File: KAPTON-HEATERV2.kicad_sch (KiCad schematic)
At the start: 18 parts, among them J1 XT60PW-M, J2 XT60PW-M, J3 1985276, J4 1985218, J5 10090926-P154XLF, K1 1-1393210-8, Q1 AO3400A, U1 TC4427ACOA

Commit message: finalized?
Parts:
- removed C1: C0.1uf, Capacitor_SMD:C_0805_2012Metric, symbol Device:C
- removed C2: C47uf, Capacitor_THT:CP_Radial_D6.3mm_P2.50mm, symbol Device:C
- removed C3: C1uf, Capacitor_SMD:C_0805_2012Metric, symbol Device:C
- added R4: 4.7k, symbol Device:R
- added R5: 10k, symbol Device:R
- C4: value C10uf -> C47.5nf; footprint Capacitor_THT:CP_Radial_D6.3mm_P2.50mm -> Capacitor_SMD:C_0805_2012Metric
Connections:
- net 10V PWM: now also R5.1
- net 5V: now also D1.1 (K); no longer D1.2 (A)
- net GND: now also R4.2, R5.2
- net at K1.2, Q1.2: now also D1.2 (A); no longer D1.1 (K)
- net at Q1.1, R1.2: now also R4.1
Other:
- note removed: "Decoupling capacitors"
- moved on the sheet: C4, D1

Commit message: forgot to save sch
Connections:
- net 5V: now also J5.11; no longer J5.10
- net GND: now also J5.10; no longer J5.11
- net TH6: now also J5.15; no longer J5.6
- net TH7: now also J5.14; no longer J5.7
- net TH8: now also J5.13; no longer J5.8
- net TH9: now also J5.12; no longer J5.9

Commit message: added resistors to pcb
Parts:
- R4, R5: footprint (none) -> PCM_JLCPCB:R_1206
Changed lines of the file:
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@@
 			)
 		)
-		(property "Footprint" ""
+		(property "Footprint" "PCM_JLCPCB:R_1206"
 			(at 144.272 95.25 90)
 			(effects
@@
 			)
 		)
-		(property "Footprint" ""
+		(property "Footprint" "PCM_JLCPCB:R_1206"
 			(at 82.042 35.56 90)
 			(effects

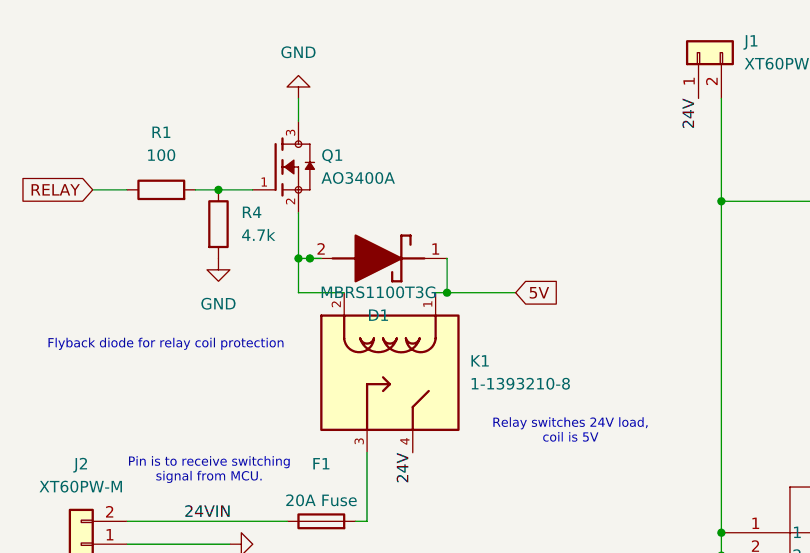
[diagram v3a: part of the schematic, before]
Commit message: fixed a trace
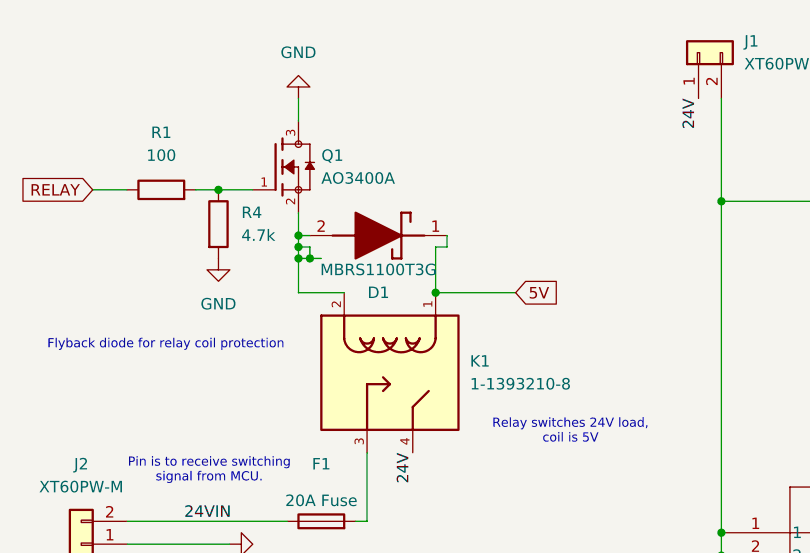
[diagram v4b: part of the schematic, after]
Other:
- moved on the sheet: D1
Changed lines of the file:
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@@
+	)
+	(junction
+		(at 107.95 43.18)
+		(diameter 0)
+		(color 0 0 0 0)
 	)
 	(junction
@@
 	)
 	(junction
-		(at 109.22 43.18)
-		(diameter 0)
-		(color 0 0 0 0)
-	)
-	(junction
 		(at 92.71 39.37)
 		(diameter 0)
@@
 	)
 	(junction
+		(at 92.71 38.1)
+		(diameter 0)
+		(color 0 0 0 0)
+	)
+	(junction
+		(at 92.71 36.83)
+		(diameter 0)
+		(color 0 0 0 0)
+	)
+	(junction
 		(at 93.98 39.37)
 		(diameter 0)
@@
 	(wire
 		(pts
+			(xy 92.71 38.1) (xy 92.71 39.37)
+		)
+		(stroke
+			(width 0)
+			(type default)
+		)
+	)
+	(wire
+		(pts
 			(xy 95.25 39.37) (xy 93.98 39.37)
 		)
@@
 	(wire
 		(pts
+			(xy 93.98 36.83) (xy 92.71 36.83)
+		)
+		(stroke
+			(width 0)
+			(type default)
+		)
+	)
+	(wire
+		(pts
 			(xy 146.05 91.44) (xy 138.43 91.44)
 		)
@@
 	(wire
 		(pts
-			(xy 107.95 43.18) (xy 109.22 43.18)
+			(xy 107.95 43.18) (xy 116.84 43.18)
 		)
 		(stroke
@@
 	(wire
 		(pts
+			(xy 92.71 38.1) (xy 93.98 38.1)
+		)
+		(stroke
+			(width 0)
+			(type default)
+		)
+	)
+	(wire
+		(pts
 			(xy 87.63 88.9) (xy 96.52 88.9)
 		)
@@
 	(wire
 		(pts
+			(xy 92.71 36.83) (xy 92.71 38.1)
+		)
+		(stroke
+			(width 0)
+			(type default)
+		)
+	)
+	(wire
+		(pts
 			(xy 100.33 68.58) (xy 99.06 68.58)
 		)
@@
 	(wire
 		(pts
+			(xy 107.95 38.1) (xy 107.95 43.18)
+		)
+		(stroke
+			(width 0)
+			(type default)
+		)
+	)
+	(wire
+		(pts
 			(xy 81.28 31.75) (xy 83.82 31.75)
 		)
@@
 	(wire
 		(pts
-			(xy 109.22 39.37) (xy 109.22 43.18)
-		)
-		(stroke
-			(width 0)
-			(type default)
-		)
-	)
-	(wire
-		(pts
-			(xy 109.22 43.18) (xy 116.84 43.18)
+			(xy 109.22 36.83) (xy 109.22 38.1)
 		)
 		(stroke
@@
 	(wire
 		(pts
+			(xy 109.22 38.1) (xy 107.95 38.1)
+		)
+		(stroke
+			(width 0)
+			(type default)
+		)
+	)
+	(wire
+		(pts
 			(xy 139.7 21.59) (xy 139.7 33.02)
 		)
@@
 	(wire
 		(pts
-			(xy 92.71 34.29) (xy 92.71 39.37)
+			(xy 92.71 34.29) (xy 92.71 36.83)
 		)
 		(stroke
@@
 		(pts
 			(xy 93.98 39.37) (xy 92.71 39.37)
+		)
+		(stroke
+			(width 0)
+			(type default)
+		)
+	)
+	(wire
+		(pts
+			(xy 93.98 38.1) (xy 93.98 39.37)
 		)
 		(stroke
@@
 	(symbol
 		(lib_id "MBRS1100T3G:MBRS1100T3G")
-		(at 111.76 39.37 180)
+		(at 111.76 36.83 180)
 		(unit 1)
 		(exclude_from_sim no)
@@
 		(dnp no)
 		(property "Reference" "D1"
-			(at 101.6 45.72 0)
+			(at 101.6 43.18 0)
 			(effects
 				(font
@@
 		)
 		(property "Value" "MBRS1100T3G"
-			(at 101.6 43.18 0)
+			(at 101.6 40.64 0)
 			(effects
 				(font
@@
 		)
 		(property "Footprint" "MBRS1100T3G:DIOM5436X247N"
-			(at 99.06 -54.28 0)
+			(at 99.06 -56.82 0)
 			(effects
 				(font
@@
 		)
 		(property "Datasheet" "https://www.onsemi.com/pub/Collateral/MBRS1100T3-D.PDF"
-			(at 99.06 -154.28 0)
+			(at 99.06 -156.82 0)
 			(effects
 				(font
@@
 		)
 		(property "Description" "Weight: 95 mg (approximately); Rectangular Package for Automated Handling; Case: Epoxy, Molded; Markings: MBRS190T3: B19 MBRS1100T3: B1C; Cathode Polarity Band; Lead and Mounting Surface Temperature for Soldering Purposes: 260C Max. for 10 Seconds; Shipped in 12 mm Tape and Reel, 2500 units per reel; 150C Operating Junction Temperature; Finish: All External Surfaces Corrosion Resistant and Terminal Leads are Readily Solderable; Small Compact Surface Mountable Package with J-Bend Leads; Highly Stable Oxide"
-			(at 111.76 39.37 0)
+			(at 111.76 36.83 0)
 			(effects
 				(font
@@
 		)
 		(property "Height" "2.47"
-			(at 99.06 -354.28 0)
+			(at 99.06 -356.82 0)
 			(effects
 				(font
@@
 		)
 		(property "Mouser Part Number" "863-MBRS1100T3G"
-			(at 99.06 -454.28 0)
+			(at 99.06 -456.82 0)
 			(effects
 				(font
@@
 		)
 		(property "Mouser Price/Stock" "https://www.mouser.co.uk/ProductDetail/onsemi/MBRS1100T3G?qs=3JMERSakebpsze4F2qcnhA%3D%3D"
-			(at 99.06 -554.28 0)
+			(at 99.06 -556.82 0)
 			(effects
 				(font
@@
 		)
 		(property "Manufacturer_Name" "onsemi"
-			(at 99.06 -654.28 0)
+			(at 99.06 -656.82 0)
 			(effects
 				(font
@@
 		)
 		(property "Manufacturer_Part_Number" "MBRS1100T3G"
-			(at 99.06 -754.28 0)
-			(effects
-				(font
+			(at 99.06 -756.82 0)
+			(effects
+				(font

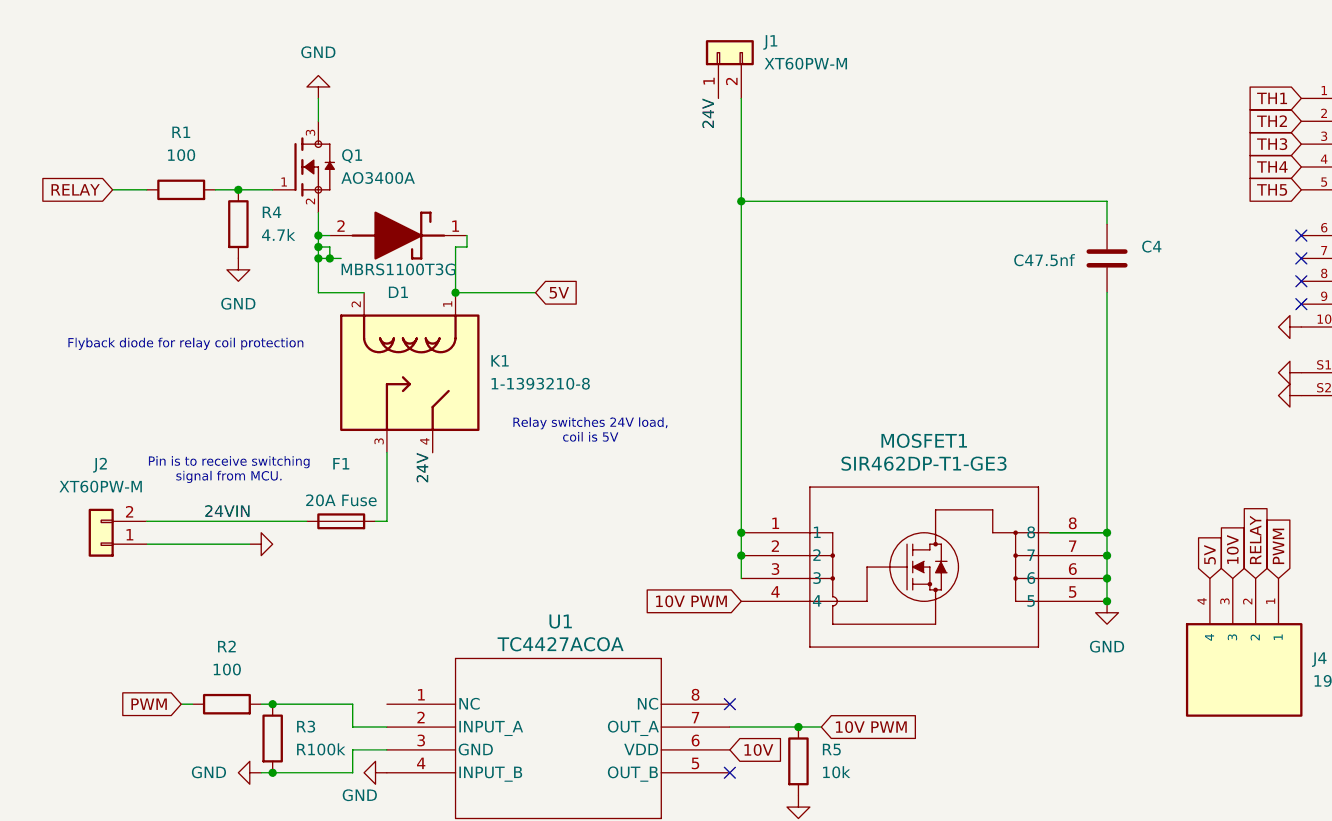
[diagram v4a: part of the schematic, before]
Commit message: fixed the mosfet
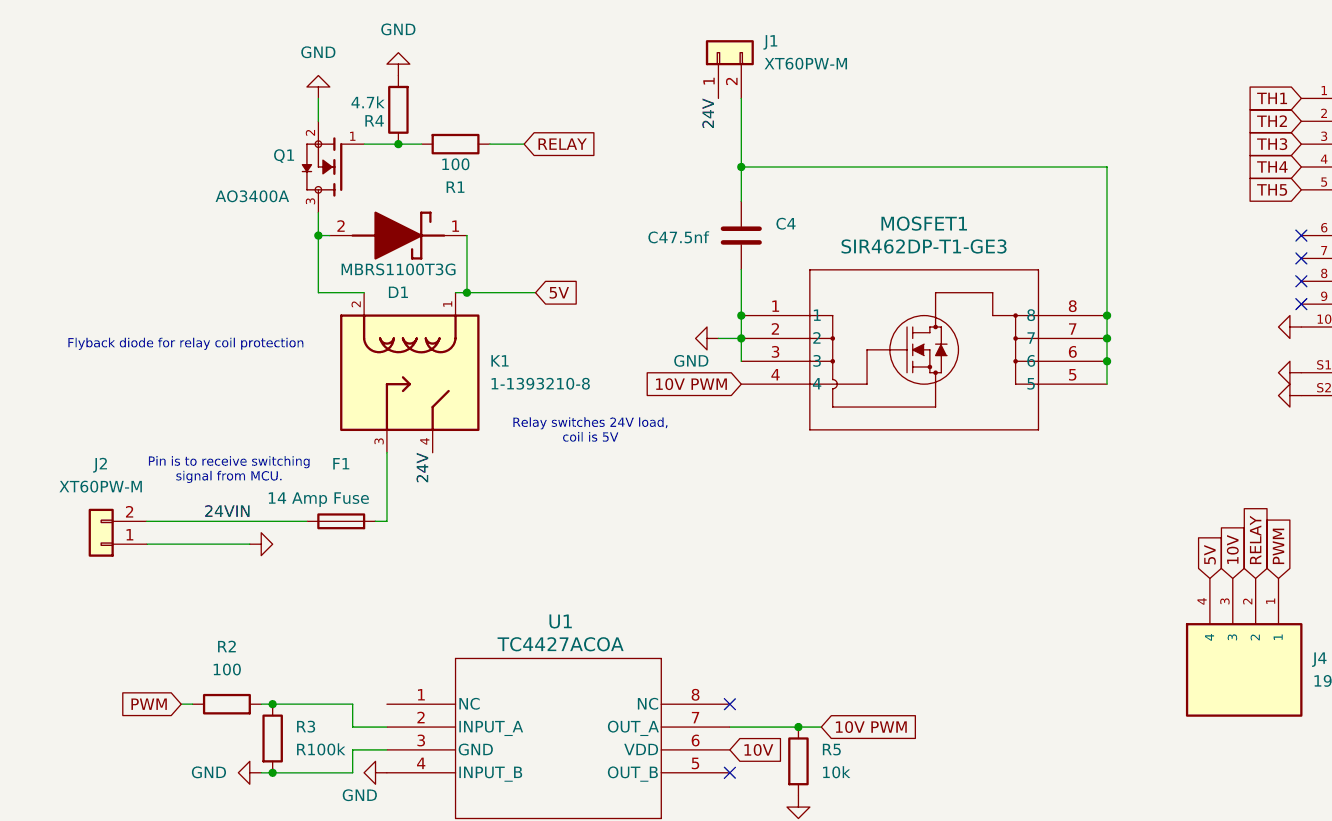
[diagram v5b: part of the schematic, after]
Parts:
- F1: value 20A Fuse -> 14 Amp Fuse
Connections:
- net GND: now also MOSFET1.1, MOSFET1.2, MOSFET1.3, Q1.2; no longer MOSFET1.5, MOSFET1.6, MOSFET1.7, MOSFET1.8, Q1.3
- net at D1.2 (A), K1.2: now also Q1.3; no longer Q1.2
- new net: C4.2, J1.2 (Pin_2), MOSFET1.5, MOSFET1.6, MOSFET1.7, MOSFET1.8
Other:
- moved on the sheet: C4, MOSFET1, Q1, R1, R4

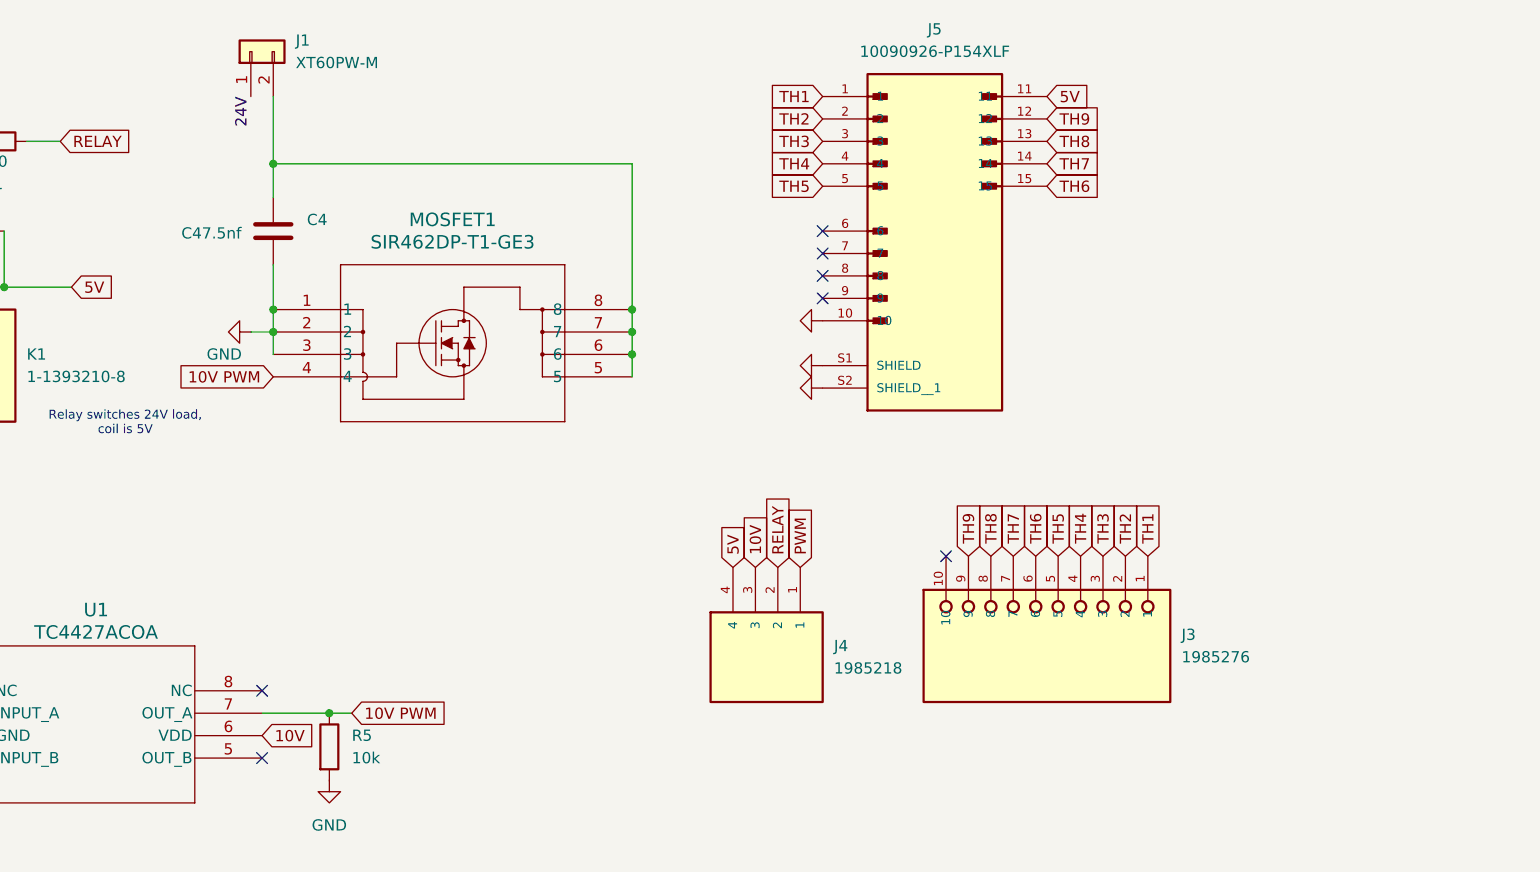
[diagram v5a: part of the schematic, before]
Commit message: added shunt resistor, fixed caps
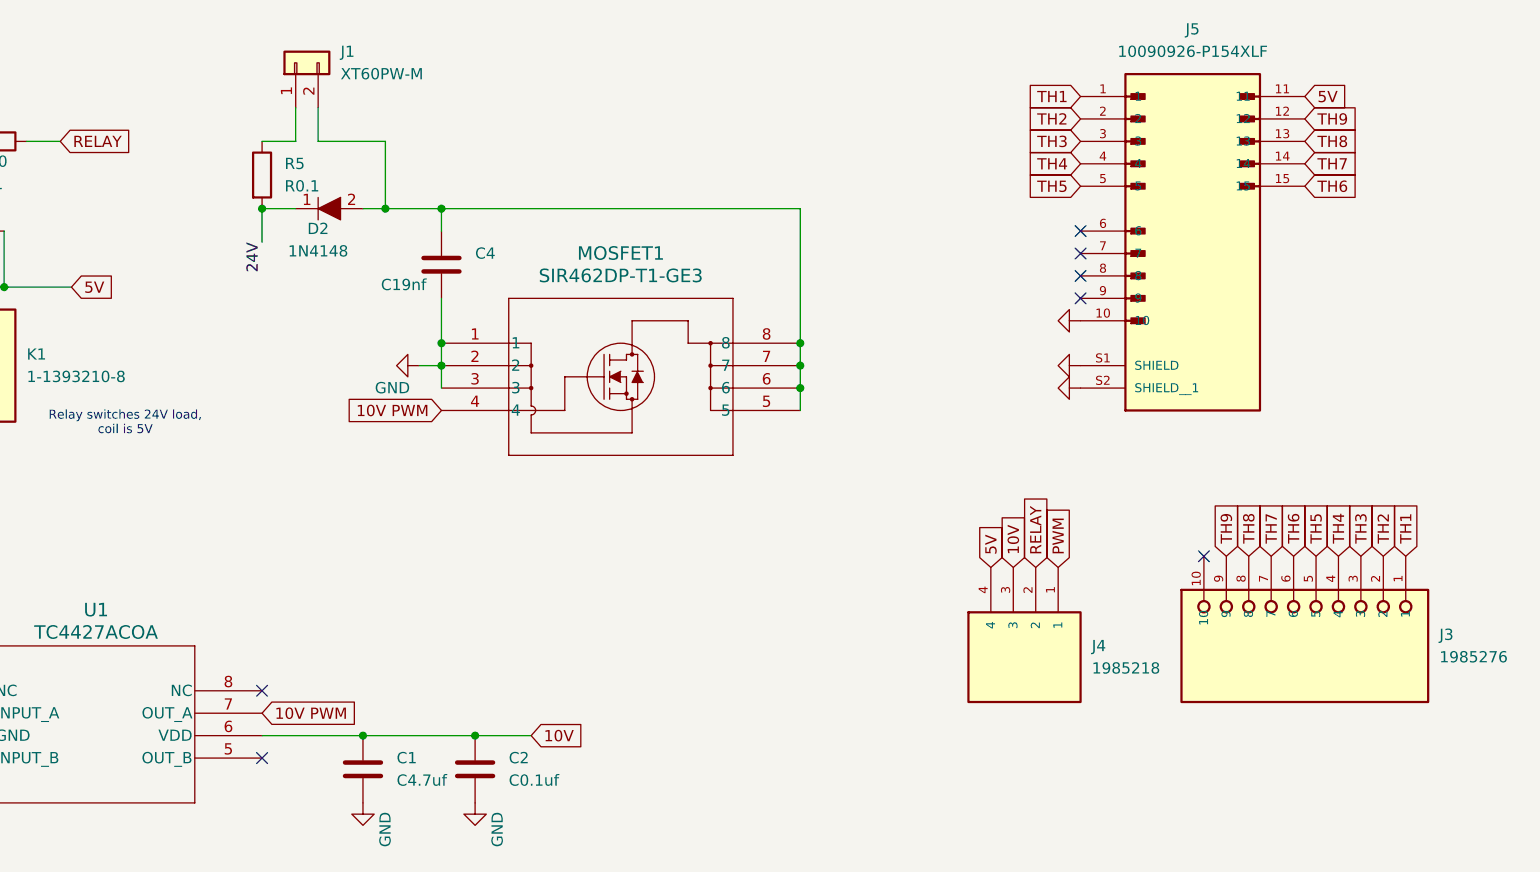
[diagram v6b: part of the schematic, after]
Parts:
- added C1: C4.7uf, symbol Device:C
- added C2: C0.1uf, symbol Device:C
- added D2: 1N4148, digikey-footprints:Diode_DO-35_P10mm, symbol dk_Diodes-Rectifiers-Single:1N4148
- C4: value C47.5nf -> C19nf
- R5: value 10k -> R0.1; footprint PCM_JLCPCB:R_1206 -> (none)
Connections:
- net 10V: now also C1.1, C2.1
- net 10V PWM: no longer R5.1
- net 24V: now also R5.2, D2.1; no longer J1.1 (Pin_1)
- net GND: now also C1.2, C2.2; no longer R5.2
- net at C4.2, J1.2 (Pin_2), MOSFET1.5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: now also D2.2
- new net: J1.1 (Pin_1), R5.1
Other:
- moved on the sheet: C4, J1, J3, J4, J5, MOSFET1

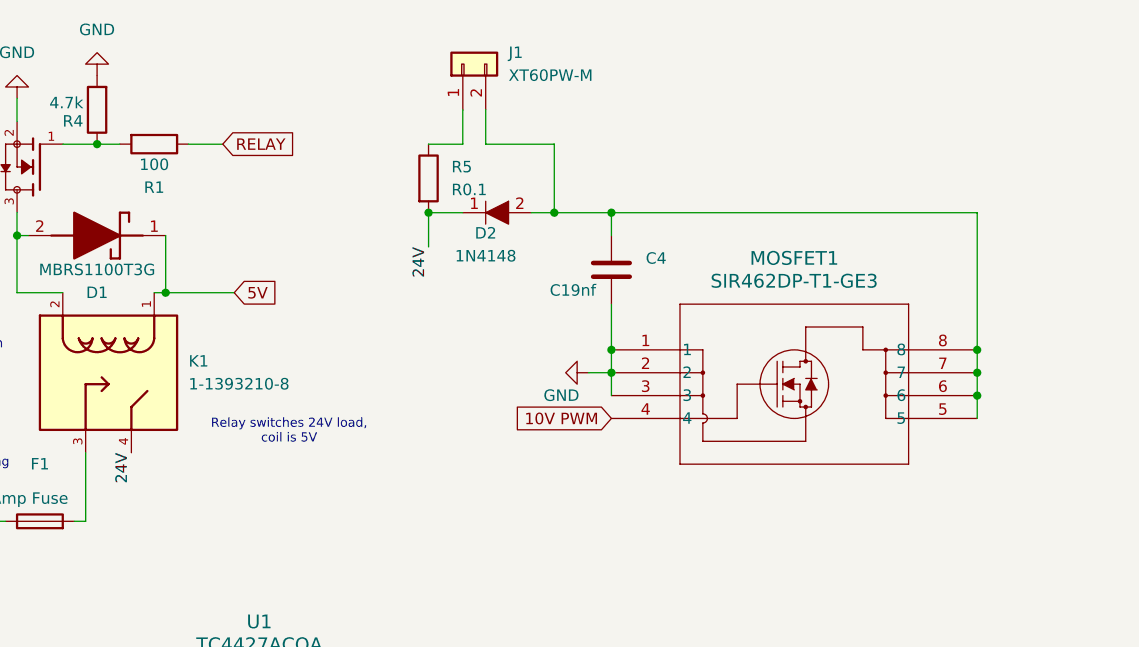
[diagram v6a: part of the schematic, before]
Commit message: edited sch, added footprints
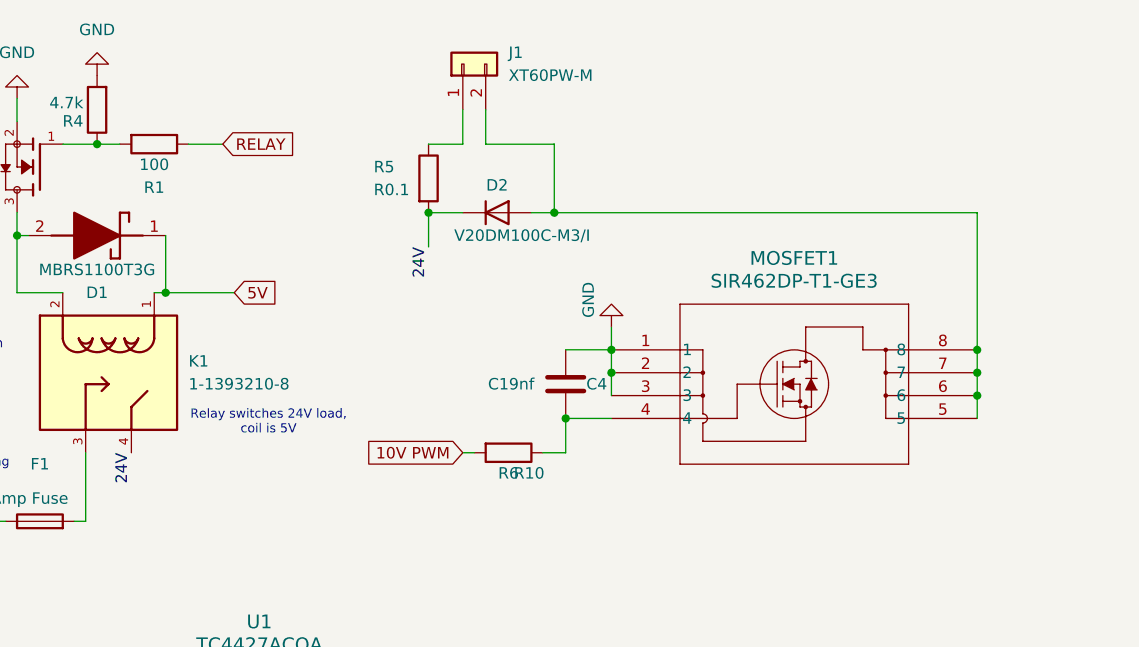
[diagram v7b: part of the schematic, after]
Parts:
- removed D2: 1N4148, digikey-footprints:Diode_DO-35_P10mm, symbol dk_Diodes-Rectifiers-Single:1N4148
- added D2: V20DM100C-M3/I, Package_TO_SOT_SMD:TO-263-2, symbol Device:D
- added R6: R10, PCM_JLCPCB:R_1206, symbol Device:R
- C1, C2: footprint (none) -> Capacitor_SMD:C_0805_2012Metric
- R5: footprint (none) -> PCM_JLCPCB:R_1206
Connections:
- net 10V PWM: now also R6.2; no longer MOSFET1.4
- net 24V: now also D2.1 (K)
- net GND: now also C4.2; no longer C4.1
- net at J1.2 (Pin_2), MOSFET1.5, MOSFET1.6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: now also D2.2 (A); no longer C4.2
- new net: C4.1, MOSFET1.4, R6.1
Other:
- moved on the sheet: C4
